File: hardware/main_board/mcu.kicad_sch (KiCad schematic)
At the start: 11 parts, among them J4 Conn_02x05_Odd_Even, J5 Conn_02x10_Odd_Even, SW2 SW_Push, U4 STM32G0B1CBTx

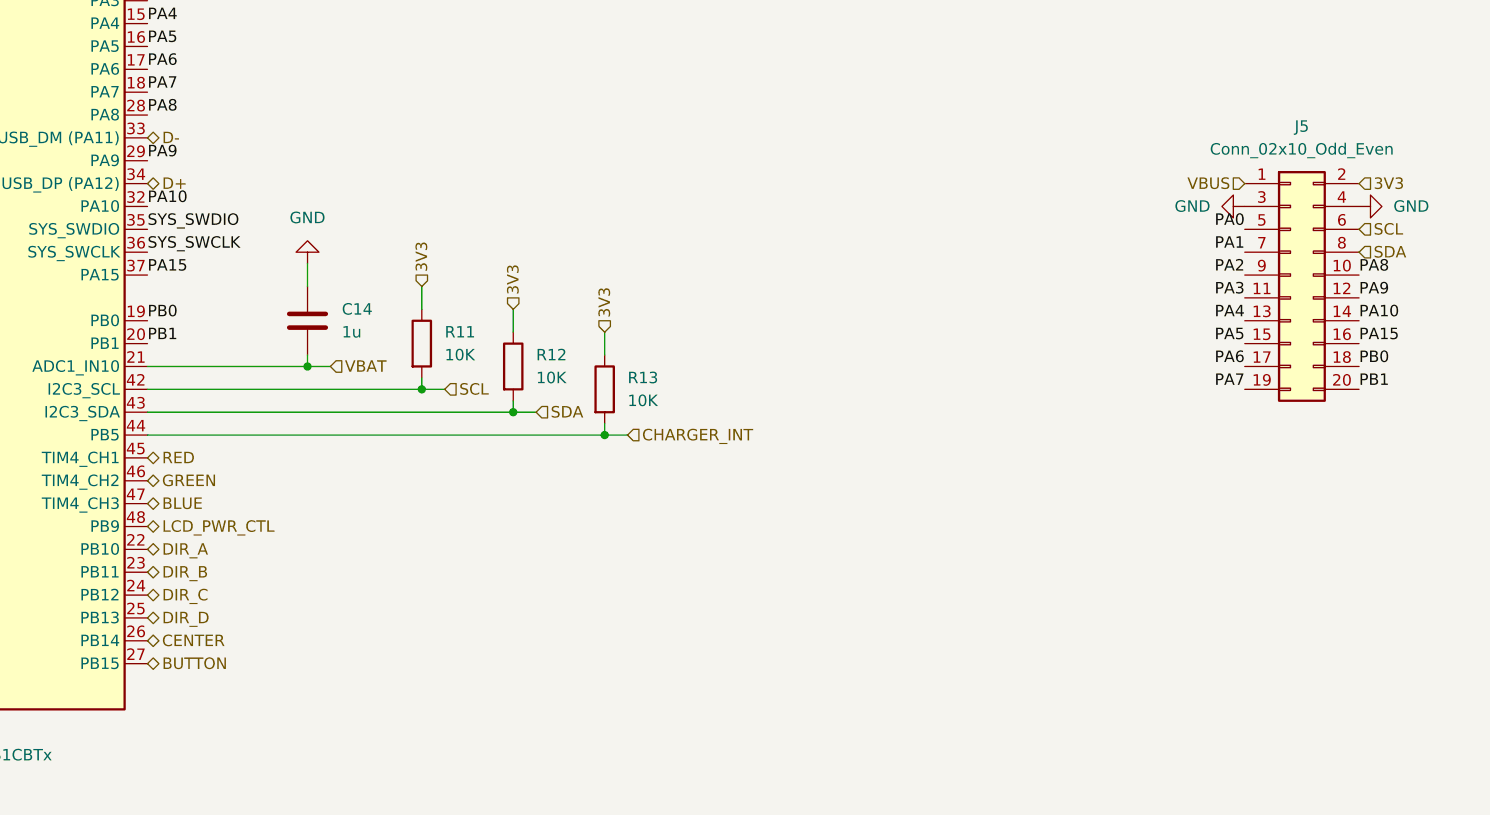
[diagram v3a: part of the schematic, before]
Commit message: Routed mainboard PCB
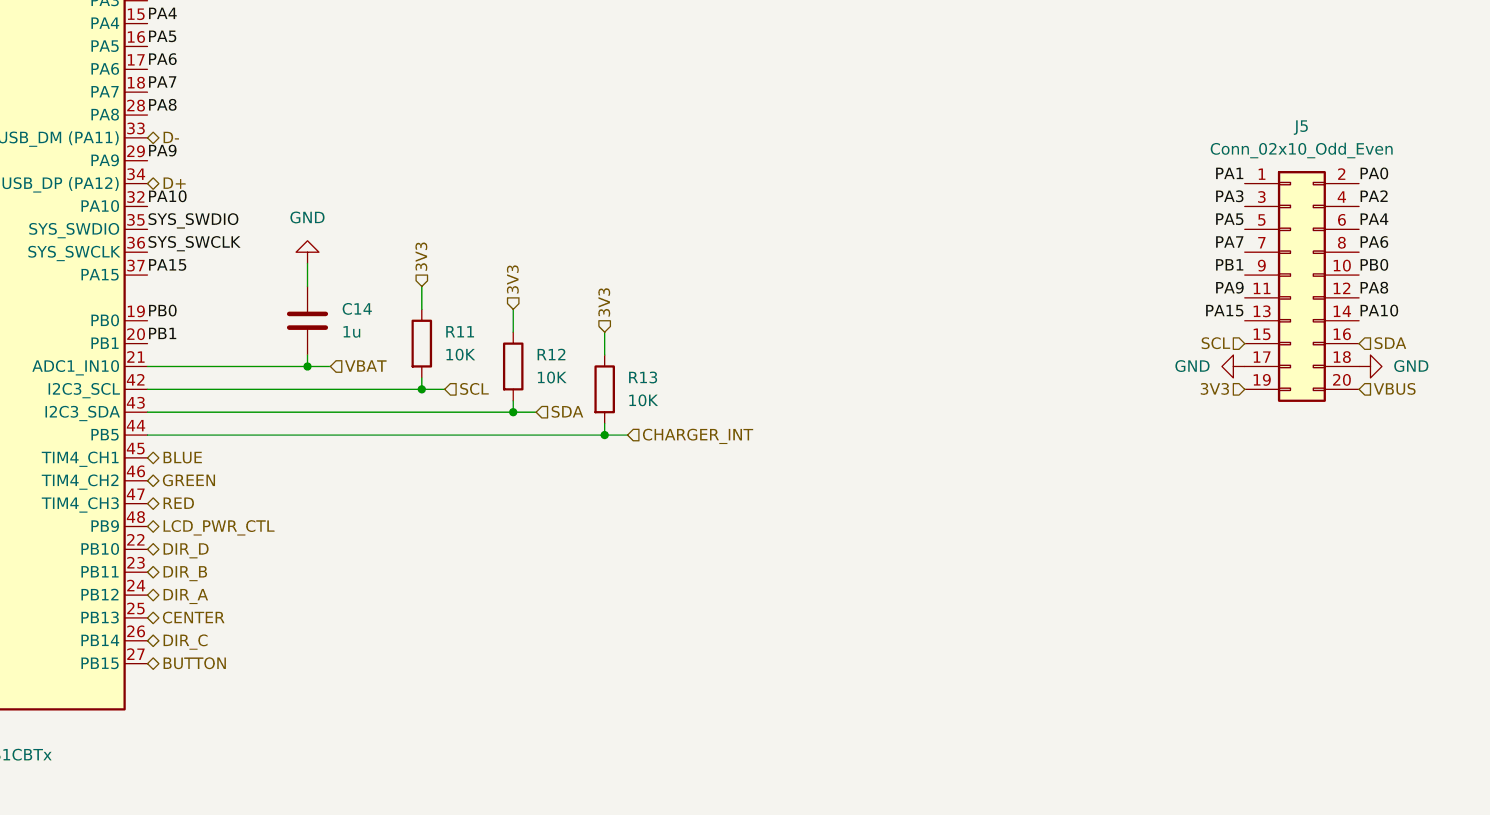
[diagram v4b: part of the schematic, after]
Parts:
- C14: footprint (none) -> Capacitor_SMD:C_0402_1005Metric
- J4: footprint Project_Footprints:SAMTEC_FTSH-105-XX-X-DV -> Project_Footprints:SAMTEC_FTSH-105-01-L-D-RA-K
- J5: footprint (none) -> Project_Footprints:SAMTEC_TSM-110-01-L-DH
- R11, R12, R13: footprint (none) -> Resistor_SMD:R_0402_1005Metric
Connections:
- net 3V3: now also J5.19 (Pin_19); no longer J5.2 (Pin_2)
- net BLUE: now also U4.45 (PB6); no longer U4.47 (PB8)
- net CENTER: now also U4.25 (PB13); no longer U4.26 (PB14)
- net DIR_A: now also U4.24 (PB12); no longer U4.22 (PB10)
- net DIR_C: now also U4.26 (PB14); no longer U4.24 (PB12)
- net DIR_D: now also U4.22 (PB10); no longer U4.25 (PB13)
- net GND: now also J5.17 (Pin_17), J5.18 (Pin_18); no longer J5.3 (Pin_3), J5.4 (Pin_4)
- net PA0: now also J5.2 (Pin_2); no longer J5.5 (Pin_5)
- net PA1: now also J5.1 (Pin_1); no longer J5.7 (Pin_7)
- net PA15: now also J5.13 (Pin_13); no longer J5.16 (Pin_16)
- net PA2: now also J5.4 (Pin_4); no longer J5.9 (Pin_9)
- net PA3: now also J5.3 (Pin_3); no longer J5.11 (Pin_11)
- net PA4: now also J5.6 (Pin_6); no longer J5.13 (Pin_13)
- net PA5: now also J5.5 (Pin_5); no longer J5.15 (Pin_15)
- net PA6: now also J5.8 (Pin_8); no longer J5.17 (Pin_17)
- net PA7: now also J5.7 (Pin_7); no longer J5.19 (Pin_19)
- net PA8: now also J5.12 (Pin_12); no longer J5.10 (Pin_10)
- net PA9: now also J5.11 (Pin_11); no longer J5.12 (Pin_12)
- net PB0: now also J5.10 (Pin_10); no longer J5.18 (Pin_18)
- net PB1: now also J5.9 (Pin_9); no longer J5.20 (Pin_20)
- net RED: now also U4.47 (PB8); no longer U4.45 (PB6)
- net SCL: now also J5.15 (Pin_15); no longer J5.6 (Pin_6)
- net SDA: now also J5.16 (Pin_16); no longer J5.8 (Pin_8)
- net VBUS: now also J5.20 (Pin_20); no longer J5.1 (Pin_1)
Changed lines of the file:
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@@
 	)
 	(label "PA0"
-		(at 231.14 87.63 180)
-		(effects
-			(font
-				(size 1.27 1.27)
-			)
-			(justify right bottom)
+		(at 243.84 82.55 0)
+		(effects
+			(font
+				(size 1.27 1.27)
+			)
+			(justify left bottom)
 		)
 	)
 	(label "PA8"
-		(at 243.84 92.71 0)
+		(at 243.84 95.25 0)
 		(effects
 			(font
@@
 	)
 	(label "PA4"
-		(at 231.14 97.79 180)
-		(effects
-			(font
-				(size 1.27 1.27)
-			)
-			(justify right bottom)
+		(at 243.84 87.63 0)
+		(effects
+			(font
+				(size 1.27 1.27)
+			)
+			(justify left bottom)
 		)
 	)
@@
 	)
 	(label "PA1"
-		(at 231.14 90.17 180)
+		(at 231.14 82.55 180)
 		(effects
 			(font
@@
 	)
 	(label "PA2"
-		(at 231.14 92.71 180)
-		(effects
-			(font
-				(size 1.27 1.27)
-			)
-			(justify right bottom)
+		(at 243.84 85.09 0)
+		(effects
+			(font
+				(size 1.27 1.27)
+			)
+			(justify left bottom)
 		)
 	)
@@
 	)
 	(label "PB0"
-		(at 243.84 102.87 0)
+		(at 243.84 92.71 0)
 		(effects
 			(font
@@
 	)
 	(label "PA5"
-		(at 231.14 100.33 180)
+		(at 231.14 87.63 180)
 		(effects
 			(font
@@
 	)
 	(label "PA6"
-		(at 231.14 102.87 180)
+		(at 243.84 90.17 0)
+		(effects
+			(font
+				(size 1.27 1.27)
+			)
+			(justify left bottom)
+		)
+	)
+	(label "PB1"
+		(at 231.14 92.71 180)
 		(effects
 			(font
@@
 		)
 	)
-	(label "PB1"
-		(at 243.84 105.41 0)
-		(effects
-			(font
-				(size 1.27 1.27)
-			)
-			(justify left bottom)
-		)
-	)
 	(label "PA15"
-		(at 243.84 100.33 0)
-		(effects
-			(font
-				(size 1.27 1.27)
-			)
-			(justify left bottom)
+		(at 231.14 97.79 180)
+		(effects
+			(font
+				(size 1.27 1.27)
+			)
+			(justify right bottom)
 		)
 	)
@@
 	)
 	(label "PA7"
-		(at 231.14 105.41 180)
+		(at 231.14 90.17 180)
 		(effects
 			(font
@@
 	)
 	(label "PA3"
-		(at 231.14 95.25 180)
+		(at 231.14 85.09 180)
 		(effects
 			(font
@@
 	)
 	(label "PA9"
-		(at 243.84 95.25 0)
-		(effects
-			(font
-				(size 1.27 1.27)
-			)
-			(justify left bottom)
+		(at 231.14 95.25 180)
+		(effects
+			(font
+				(size 1.27 1.27)
+			)
+			(justify right bottom)
 		)
 	)
 	(hierarchical_label "DIR_C"
 		(shape bidirectional)
-		(at 109.22 128.27 0)
+		(at 109.22 133.35 0)
 		(effects
 			(font
@@
 	(hierarchical_label "CENTER"
 		(shape bidirectional)
-		(at 109.22 133.35 0)
+		(at 109.22 130.81 0)
 		(effects
 			(font
@@
 	(hierarchical_label "BLUE"
 		(shape bidirectional)
-		(at 109.22 118.11 0)
+		(at 109.22 113.03 0)
 		(effects
 			(font
@@
 	(hierarchical_label "SCL"
 		(shape input)
-		(at 243.84 87.63 0)
-		(effects
-			(font
-				(size 1.27 1.27)
-			)
-			(justify left)
+		(at 231.14 100.33 180)
+		(effects
+			(font
+				(size 1.27 1.27)
+			)
+			(justify right)
 		)
 	)
 	(hierarchical_label "SDA"
 		(shape input)
-		(at 243.84 90.17 0)
+		(at 243.84 100.33 0)
 		(effects
 			(font
@@
 	(hierarchical_label "VBUS"
 		(shape input)
-		(at 231.14 82.55 180)
-		(effects
-			(font
-				(size 1.27 1.27)
-			)
-			(justify right)
+		(at 243.84 105.41 0)
+		(effects
+			(font
+				(size 1.27 1.27)
+			)
+			(justify left)
 		)
 	)
@@
 	(hierarchical_label "DIR_A"
 		(shape bidirectional)
-		(at 109.22 123.19 0)
+		(at 109.22 128.27 0)
 		(effects
 			(font
@@
 	(hierarchical_label "DIR_D"
 		(shape bidirectional)
-		(at 109.22 130.81 0)
+		(at 109.22 123.19 0)
 		(effects
 			(font
@@
 	(hierarchical_label "RED"
 		(shape bidirectional)
-		(at 109.22 113.03 0)
+		(at 109.22 118.11 0)
 		(effects
 			(font
@@
 	(hierarchical_label "3V3"
 		(shape input)
-		(at 243.84 82.55 0)
-		(effects
-			(font
-				(size 1.27 1.27)
-			)
-			(justify left)
+		(at 231.14 105.41 180)
+		(effects
+			(font
+				(size 1.27 1.27)
+			)
+			(justify right)
 		)
 	)
@@
 			)
 		)
-		(property "Footprint" ""
+		(property "Footprint" "Resistor_SMD:R_0402_1005Metric"
 			(at 137.922 100.33 90)
 			(effects
@@
 		(dnp no)
 		(fields_autoplaced yes)
-		(property "Reference" "#PWR025"
+		(property "Reference" "#PWR26"
 			(at 224.79 40.64 0)
 			(effects
@@
 			(project ""
 				(path "/e7586151-38a0-41a9-9cce-542cfb7665db/1a2b55f4-c1fd-4586-87d2-eefd04e93091"
-					(reference "#PWR025")
+					(reference "#PWR26")
 					(unit 1)
 				)
@@
 	(symbol
 		(lib_id "power:GND")
-		(at 243.84 85.09 90)
+		(at 243.84 102.87 90)
+		(mirror x)
 		(unit 1)
 		(exclude_from_sim no)
@@
 		(on_board yes)
 		(dnp no)
-		(property "Reference" "#PWR027"
-			(at 250.19 85.09 0)
+		(property "Reference" "#PWR28"
+			(at 250.19 102.87 0)
 			(effects
 				(font
@@
 		)
 		(property "Value" "GND"
-			(at 247.65 85.0901 90)
+			(at 247.65 102.8699 90)
 			(effects
 				(font
@@
 		)
 		(property "Footprint" ""
-			(at 243.84 85.09 0)
+			(at 243.84 102.87 0)
 			(effects
 				(font
@@
 		)
 		(property "Datasheet" ""
-			(at 243.84 85.09 0)
+			(at 243.84 102.87 0)
 			(effects
 				(font
@@
 		)
 		(property "Description" "Power symbol creates a global label with name \"GND\" , ground"
-			(at 243.84 85.09 0)
+			(at 243.84 102.87 0)
 			(effects
 				(font
@@
 			(project "main_board"
 				(path "/e7586151-38a0-41a9-9cce-542cfb7665db/1a2b55f4-c1fd-4586-87d2-eefd04e93091"
-					(reference "#PWR027")
+					(reference "#PWR28")
 					(unit 1)
 				)
@@
 	(symbol
 		(lib_id "power:GND")
-		(at 231.14 85.09 270)
+		(at 231.14 102.87 270)
+		(mirror x)
 		(unit 1)
 		(exclude_from_sim no)
@@
 		(dnp no)
 		(fields_autoplaced yes)
-		(property "Reference" "#PWR026"
-			(at 224.79 85.09 0)
+		(property "Reference" "#PWR27"
+			(at 224.79 102.87 0)
 			(effects
 				(font
@@
 		)
 		(property "Value" "GND"
-			(at 227.33 85.0899 90)
+			(at 227.33 102.8701 90)
 			(effects
 				(font
@@
 		)
 		(property "Footprint" ""
-			(at 231.14 85.09 0)
+			(at 231.14 102.87 0)
 			(effects
 				(font
@@
 		)
 		(property "Datasheet" ""
-			(at 231.14 85.09 0)
+			(at 231.14 102.87 0)
 			(effects
 				(font
@@
 		)
 		(property "Description" "Power symbol creates a global label with name \"GND\" , ground"
-			(at 231.14 85.09 0)
+			(at 231.14 102.87 0)
 			(effects
 				(font
@@
 			(project "main_board"
 				(path "/e7586151-38a0-41a9-9cce-542cfb7665db/1a2b55f4-c1fd-4586-87d2-eefd04e93091"
-					(reference "#PWR026")
+					(reference "#PWR27")
 					(unit 1)
 				)
@@
 		(dnp no)
 		(fields_autoplaced yes)
-		(property "Reference" "#PWR021"
+		(property "Reference" "#PWR22"
 			(at 78.74 20.32 0)
 			(effects
@@
 			(project "main_board"
 				(path "/e7586151-38a0-41a9-9cce-542cfb7665db/1a2b55f4-c1fd-4586-87d2-eefd04e93091"
-					(reference "#PWR021")
+					(reference "#PWR22")
 					(unit 1)
 				)
@@
 		(dnp no)
 		(fields_autoplaced yes)
-		(property "Reference" "#PWR020"
+		(property "Reference" "#PWR21"
 			(at 24.13 73.66 0)
 			(effects
@@
 			(project "main_board"
 				(path "/e7586151-38a0-41a9-9cce-542cfb7665db/1a2b55f4-c1fd-4586-87d2-eefd04e93091"
-					(reference "#PWR020")
+					(reference "#PWR21")
 					(unit 1)
 				)
@@
 			)
 		)
-		(property "Footprint" ""
+		(property "Footprint" "Project_Footprints:SAMTEC_TSM-110-01-L-DH"
 			(at 236.22 92.71 0)
 			(effects
@@
 		(dnp no)
 		(fields_autoplaced yes)
-		(property "Reference" "#PWR022"
+		(property "Reference" "#PWR23"
 			(at 81.28 153.67 0)
 			(effects
@@
 			(project "main_board"
 				(path "/e7586151-38a0-41a9-9cce-542cfb7665db/1a2b55f4-c1fd-4586-87d2-eefd04e93091"
-					(reference "#PWR022")
+					(reference "#PWR23")
 					(unit 1)
 				)
@@
 		(dnp no)
 		(fields_autoplaced yes)
-		(property "Reference" "#PWR023"
+		(property "Reference" "#PWR24"
 			(at 127 85.09 0)
 			(effects
@@
 			(project "main_board"
 				(path "/e7586151-38a0-41a9-9cce-542cfb7665db/1a2b55f4-c1fd-4586-87d2-eefd04e93091"
-					(reference "#PWR023")
+					(reference "#PWR24")
 					(unit 1)
 				)
@@
 			)
 		)
-		(property "Footprint" ""
+		(property "Footprint" "Resistor_SMD:R_0402_1005Metric"
 			(at 158.242 105.41 90)
 			(effects
@@
 			)
 		)
-		(property "Footprint" ""
+		(property "Footprint" "Resistor_SMD:R_0402_1005Metric"
 			(at 148.082 102.87 90)
 			(effects
@@
 		(dnp no)
 		(fields_autoplaced yes)
-		(property "Reference" "#PWR024"
+		(property "Reference" "#PWR25"
 			(at 224.79 38.1 0)
 			(effects
@@
 			(project ""
 				(path "/e7586151-38a0-41a9-9cce-542cfb7665db/1a2b55f4-c1fd-4586-87d2-eefd04e93091"
-					(reference "#PWR024")
+					(reference "#PWR25")
 					(unit 1)
 				)
@@
 			)
 		)
-		(property "Footprint" ""
+		(property "Footprint" "Capacitor_SMD:C_0402_1005Metric"
 			(at 127.9652 101.6 0)
 			(effects
@@
 			)
 		)
-		(property "Footprint" "Project_Footprints:SAMTEC_FTSH-105-XX-X-DV"
+		(property "Footprint" "Project_Footprints:SAMTEC_FTSH-105-01-L-D-RA-K"
 			(at 236.22 40.64 0)
 			(effects

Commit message: Update component IDs
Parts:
- C11, C13: JLCPCB (none) -> C1525
- C12: JLCPCB (none) -> C23733
- C14: JLCPCB (none) -> C52923
- R11, R12, R13: value 10K -> 10k; JLCPCB (none) -> C25744
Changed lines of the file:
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@@
 			)
 		)
-		(property "Value" "10K"
+		(property "Value" "10k"
 			(at 142.24 101.5999 0)
 			(effects
@@
 		)
 		(property "Description" "Resistor"
+			(at 139.7 100.33 0)
+			(effects
+				(font
+					(size 1.27 1.27)
+				)
+				(hide yes)
+			)
+		)
+		(property "JLCPCB" "C25744"
 			(at 139.7 100.33 0)
 			(effects
@@
 			)
 		)
-		(property "Value" "10K"
+		(property "Value" "10k"
 			(at 162.56 106.6799 0)
 			(effects
@@
 			)
 		)
+		(property "JLCPCB" "C25744"
+			(at 160.02 105.41 0)
+			(effects
+				(font
+					(size 1.27 1.27)
+				)
+				(hide yes)
+			)
+		)
 		(pin "2"
 		)
@@
 			)
 		)
-		(property "Value" "10K"
+		(property "Value" "10k"
 			(at 152.4 104.1399 0)
 			(effects
@@
 			)
 		)
+		(property "JLCPCB" "C25744"
+			(at 149.86 102.87 0)
+			(effects
+				(font
+					(size 1.27 1.27)
+				)
+				(hide yes)
+			)
+		)
 		(pin "2"
 		)
@@
 			)
 		)
+		(property "JLCPCB" "C52923"
+			(at 127 97.79 0)
+			(effects
+				(font
+					(size 1.27 1.27)
+				)
+				(hide yes)
+			)
+		)
 		(pin "2"
 		)
@@
 			)
 		)
+		(property "JLCPCB" "C23733"
+			(at 73.66 34.29 0)
+			(effects
+				(font
+					(size 1.27 1.27)
+				)
+				(hide yes)
+			)
+		)
 		(pin "1"
 		)
@@
 			)
 		)
+		(property "JLCPCB" "C1525"
+			(at 83.82 34.29 0)
+			(effects
+				(font
+					(size 1.27 1.27)
+				)
+				(hide yes)
+			)
+		)
 		(pin "1"
 		)
@@
 			(at 34.29 73.66 0)
 			(effects
+				(font
+					(size 1.27 1.27)
+				)
+				(hide yes)
+			)
+		)
+		(property "JLCPCB" "C1525"
+			(at 34.29 73.66 0)
+			(effects
